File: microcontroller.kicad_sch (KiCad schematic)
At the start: 4 parts, among them CN4 Samtec FTSH-107-01-L-DV-K, CN5 M20-9990346, U2 STM32H743VIT6, U3 Microchip 24AA256UIDT-I/ST

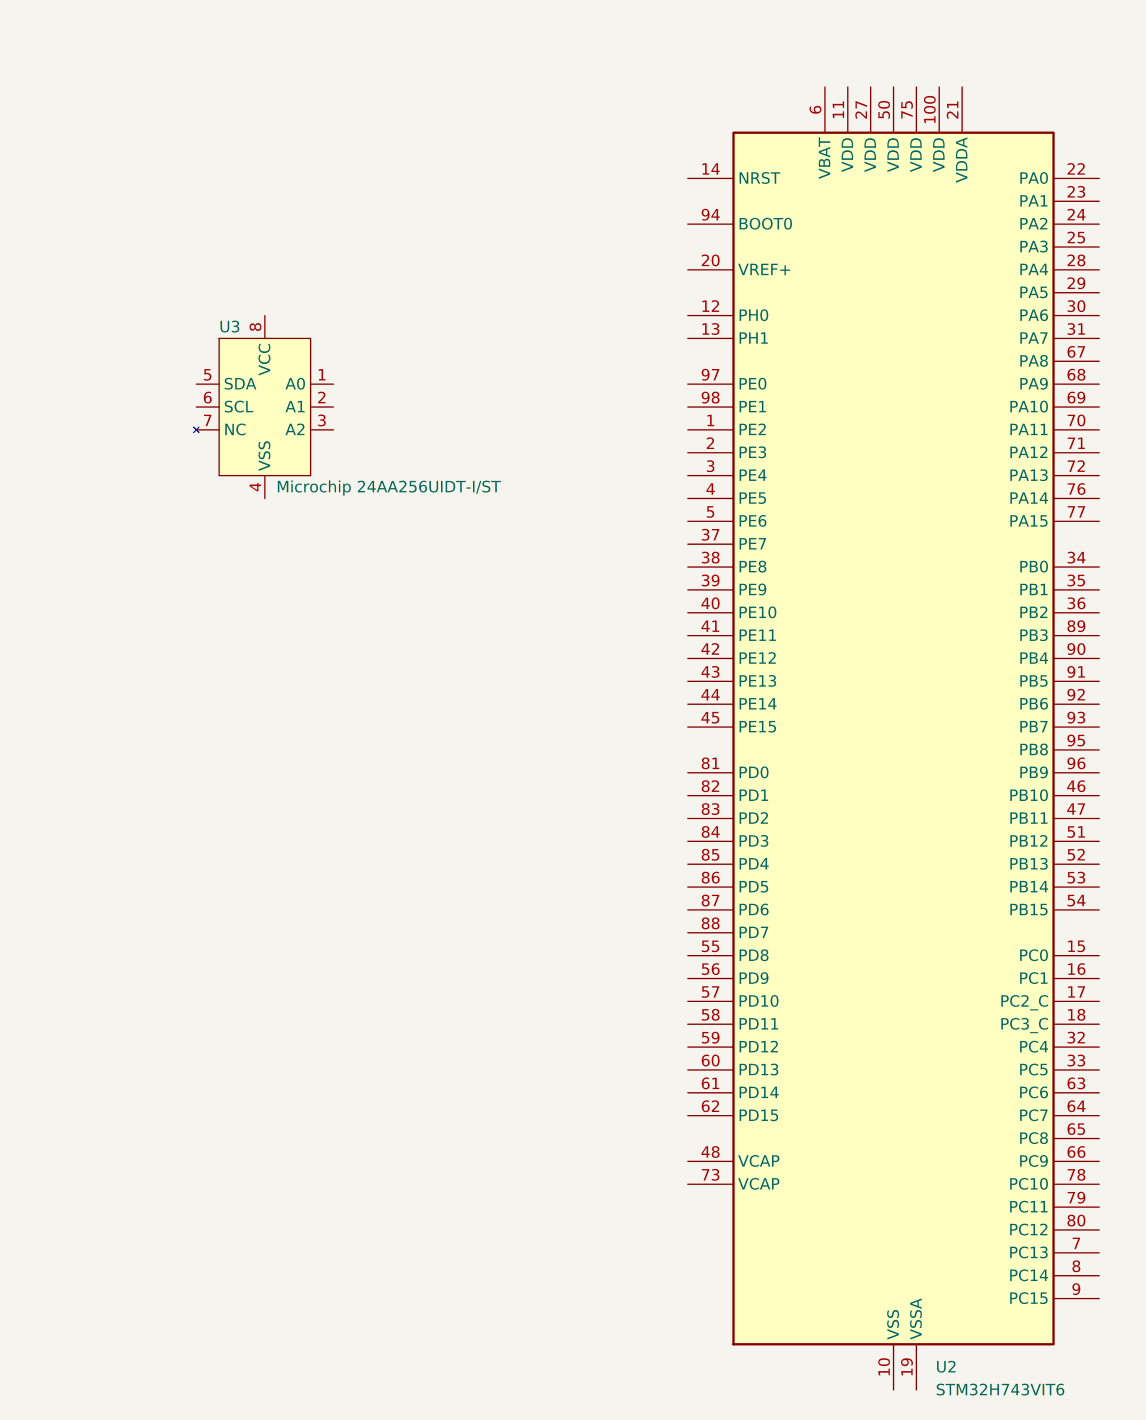
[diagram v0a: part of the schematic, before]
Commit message: started on DCDC section
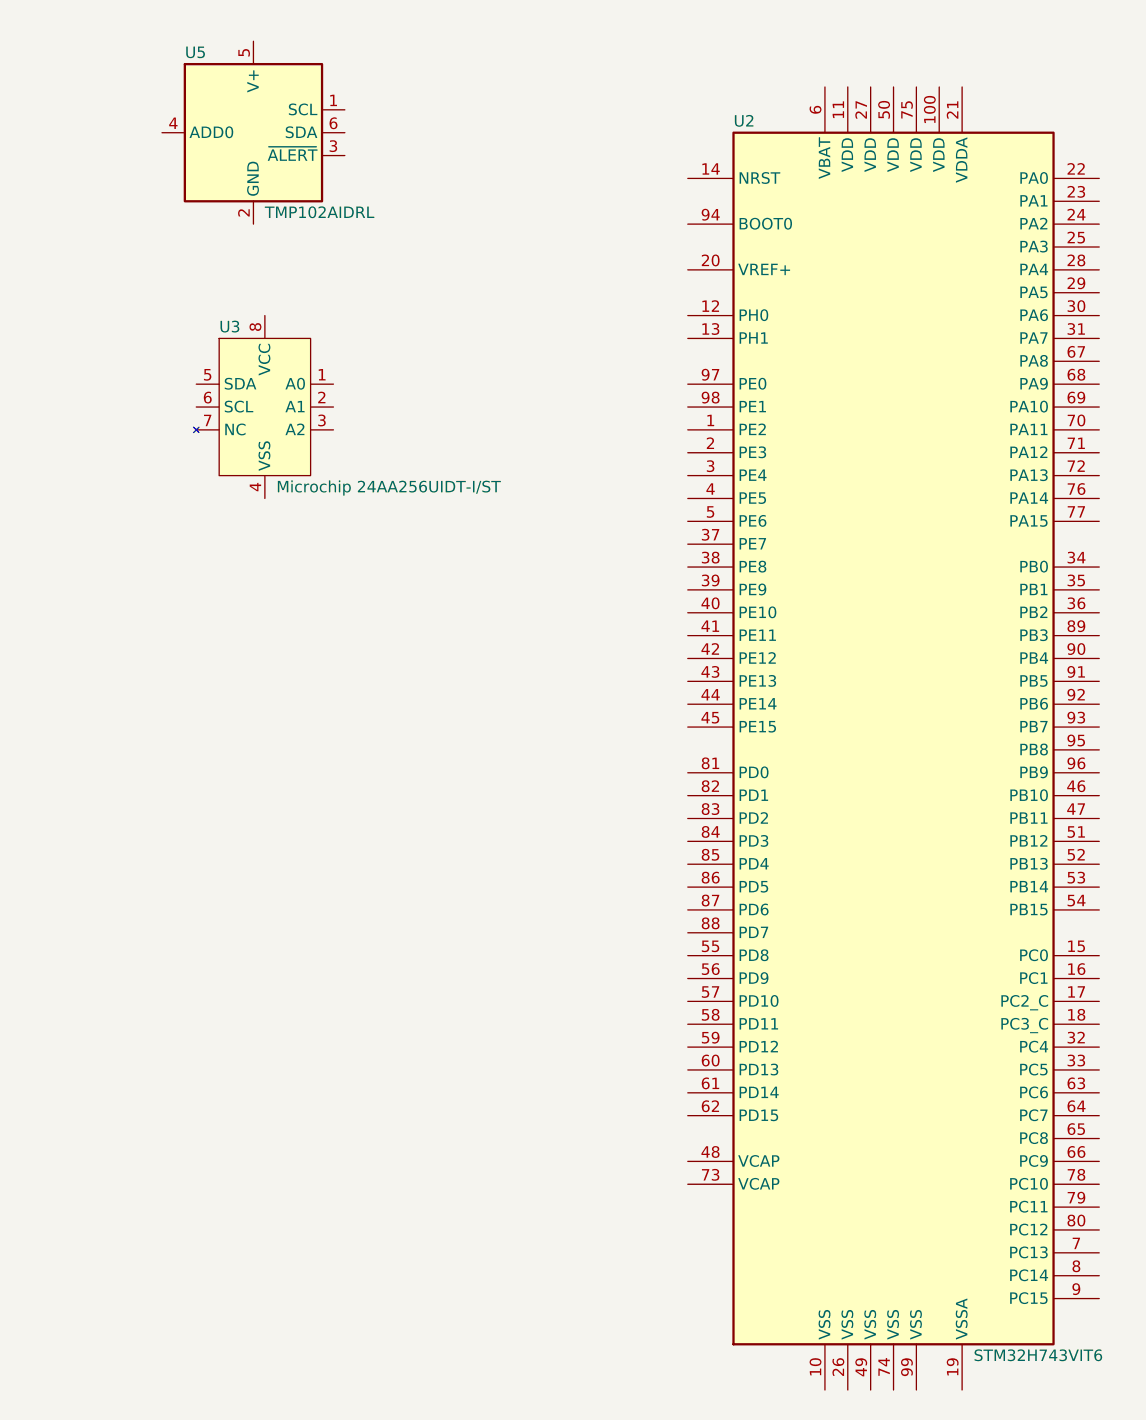
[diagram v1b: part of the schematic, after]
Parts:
- added U5: TMP102AIDRL, IC_WUT:SOT-563, symbol IC_WUT:TMP102AIDRL
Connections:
- now unconnected: U2.10 (VSS), U2.26 (VSS), U2.49 (VSS), U2.74 (VSS), U2.99 (VSS)
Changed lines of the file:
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@@
 		(fields_autoplaced yes)
 		(property "Reference" "U2"
-			(at 210.4233 209.55 0)
-			(show_name no)
-			(do_not_autoplace no)
+			(at 187.96 71.12 0)
+			(show_name no)
+			(do_not_autoplace yes)
 			(effects
 				(font
@@
 		)
 		(property "Value" "STM32H743VIT6"
-			(at 210.4233 212.09 0)
-			(show_name no)
-			(do_not_autoplace no)
+			(at 214.63 208.28 0)
+			(show_name no)
+			(do_not_autoplace yes)
 			(effects
 				(font
@@
 					(unit 1)
 				)
+			)
+		)
+	)
+	(symbol
+		(lib_id "IC_WUT:TMP102AIDRL")
+		(at 134.62 72.39 0)
+		(unit 1)
+		(body_style 1)
+		(exclude_from_sim no)
+		(in_bom yes)
+		(on_board yes)
+		(in_pos_files yes)
+		(dnp no)
+		(fields_autoplaced yes)
+		(property "Reference" "U5"
+			(at 127 63.5 0)
+			(show_name no)
+			(do_not_autoplace yes)
+			(effects
+				(font
+					(size 1.27 1.27)
+				)
+				(justify left)
+			)
+		)
+		(property "Value" "TMP102AIDRL"
+			(at 135.89 81.28 0)
+			(show_name no)
+			(do_not_autoplace yes)
+			(effects
+				(font
+					(size 1.27 1.27)
+				)
+				(justify left)
+			)
+		)
+		(property "Footprint" "IC_WUT:SOT-563"
+			(at 135.89 81.28 0)
+			(hide yes)
+			(show_name no)
+			(do_not_autoplace no)
+			(effects
+				(font
+					(size 1.27 1.27)
+				)
+				(justify left)
+			)
+		)
+		(property "Datasheet" "https://www.ti.com/lit/ds/symlink/tmp102.pdf"
+			(at 135.89 83.82 0)
+			(hide yes)
+			(show_name no)
+			(do_not_autoplace no)
+			(effects
+				(font
+					(size 1.27 1.27)
+				)
+				(justify left)
+			)
+		)
+		(property "Description" "Digital Temperature Sensor, ±3°C, low-Power, SMBus, 12 bit, Two-Wire Serial Interface, SOT-563"
+			(at 134.62 72.39 0)
+			(hide yes)
+			(show_name no)
+			(do_not_autoplace no)
+			(effects
+				(font
+					(size 1.27 1.27)
+				)
+			)
+		)
+		(property "Manufacturer" "Texas Instruments"
+			(at 134.62 72.39 0)
+			(hide yes)
+			(show_name no)
+			(do_not_autoplace no)
+			(effects
+				(font
+					(size 1.27 1.27)
+				)
+			)
+		)
+		(property "MPN" "TMP102AIDRL"
+			(at 134.62 72.39 0)
+			(hide yes)
+			(show_name no)
+			(do_not_autoplace no)
+			(effects
+				(font
+					(size 1.27 1.27)
+				)
+			)
+		)
+		(property "JLCPCB Order #" "C99269"
+			(at 134.62 72.39 0)
+			(hide yes)
+			(show_name no)
+			(do_not_autoplace no)
+			(effects
+				(font
+					(size 1.27 1.27)
+				)
+			)
+		)
+		(pin "3"
+		)
+		(pin "5"
+		)
+		(pin "4"
+		)
+		(pin "6"
+		)
+		(pin "2"
+		)
+		(pin "1"
+		)
+		(instances
+			(project "P0004-PCB-001"
+				(path "/acdb93e6-9aa6-4a78-8a68-9d0ae3318f45/a36ad431-c50e-45e1-982c-a7ffb7390ea7"
+					(reference "U5")
+					(unit 1)
+				)

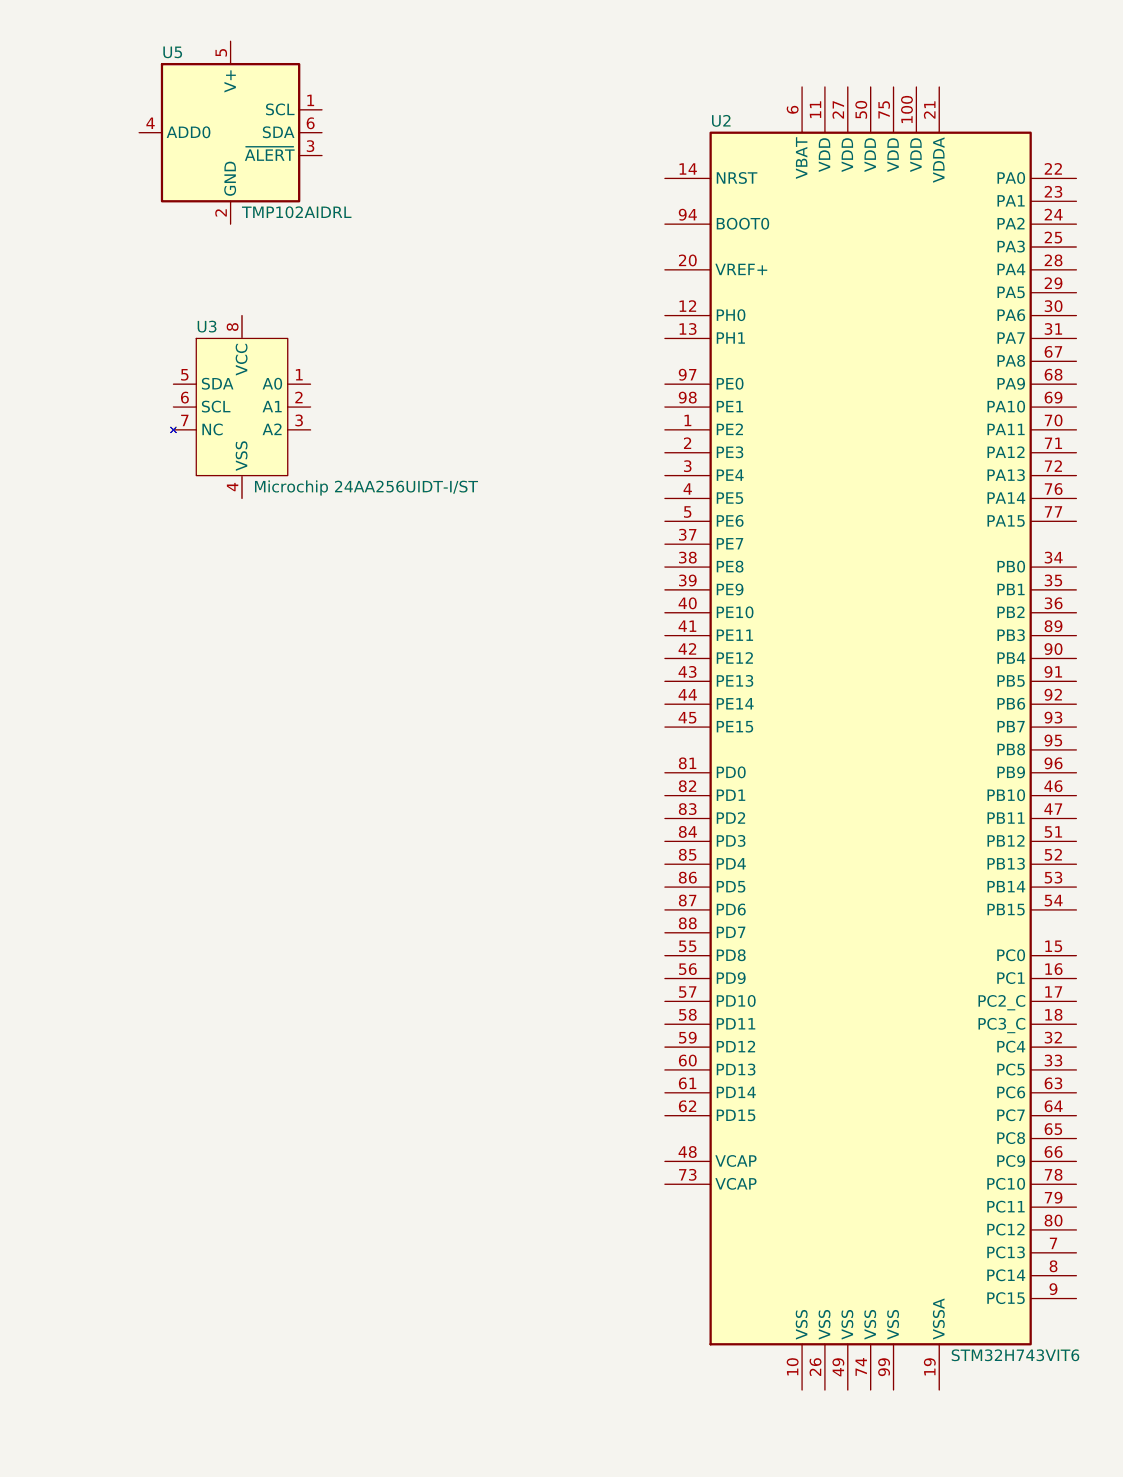
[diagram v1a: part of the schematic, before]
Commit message: added ethernet phy
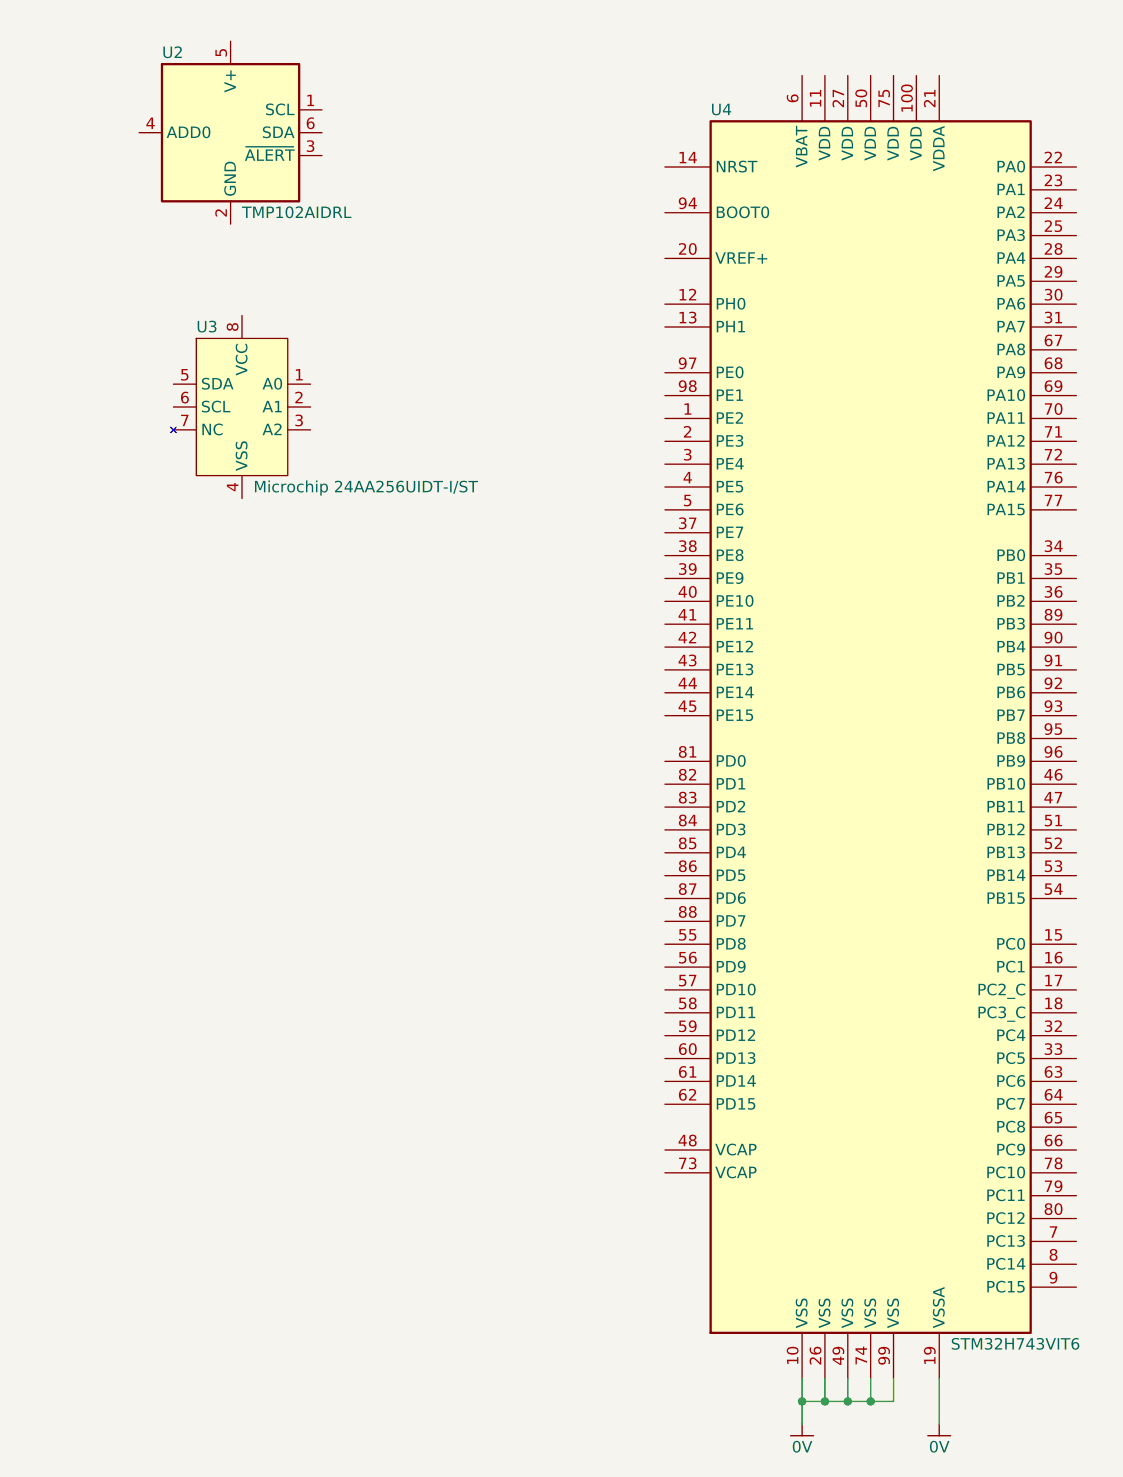
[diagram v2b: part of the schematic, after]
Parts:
- renumbered U5 to U2, U2 to U4
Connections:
- net 0V: now reaches U4.10 (VSS)
- net 0V: now also U4.19 (VSSA), U4.26 (VSS), U4.49 (VSS), U4.74 (VSS), U4.99 (VSS)
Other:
- moved on the sheet: U4
